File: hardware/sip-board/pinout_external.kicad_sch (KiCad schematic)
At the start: 24 parts, among them J2 Conn_01x10_Pin, J3 Conn_01x10_Pin, J4 Conn_01x10_Pin, J5 Conn_01x10_Pin

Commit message: WE REDOIN PCB
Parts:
- U10, U11, U12, U13, U4, U5, U6, U7, U8, U9: MPN (none) -> NXB0104GU12X
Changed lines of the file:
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@@
 			)
 		)
+		(property "MPN" "NXB0104GU12X"
+			(at 31.75 76.2 0)
+			(effects
+				(font
+					(size 1.27 1.27)
+				)
+				(hide yes)
+			)
+		)
 		(pin "5"
 		)
@@
 			)
 		)
+		(property "MPN" "NXB0104GU12X"
+			(at 118.11 144.78 0)
+			(effects
+				(font
+					(size 1.27 1.27)
+				)
+				(hide yes)
+			)
+		)
 		(pin "5"
 		)
@@
 			)
 		)
+		(property "MPN" "NXB0104GU12X"
+			(at 30.48 110.49 0)
+			(effects
+				(font
+					(size 1.27 1.27)
+				)
+				(hide yes)
+			)
+		)
 		(pin "5"
 		)
@@
 			)
 		)
+		(property "MPN" "NXB0104GU12X"
+			(at 119.38 110.49 0)
+			(effects
+				(font
+					(size 1.27 1.27)
+				)
+				(hide yes)
+			)
+		)
 		(pin "5"
 		)
@@
 			)
 		)
+		(property "MPN" "NXB0104GU12X"
+			(at 121.92 41.91 0)
+			(effects
+				(font
+					(size 1.27 1.27)
+				)
+				(hide yes)
+			)
+		)
 		(pin "5"
 		)
@@
 			)
 		)
+		(property "MPN" "NXB0104GU12X"
+			(at 120.65 76.2 0)
+			(effects
+				(font
+					(size 1.27 1.27)
+				)
+				(hide yes)
+			)
+		)
 		(pin "5"
 		)
@@
 			)
 		)
+		(property "MPN" "NXB0104GU12X"
+			(at 31.75 179.07 0)
+			(effects
+				(font
+					(size 1.27 1.27)
+				)
+				(hide yes)
+			)
+		)
 		(pin "5"
 		)
@@
 			)
 		)
+		(property "MPN" "NXB0104GU12X"
+			(at 33.02 41.91 0)
+			(effects
+				(font
+					(size 1.27 1.27)
+				)
+				(hide yes)
+			)
+		)
 		(pin "5"
 		)
@@
 			)
 		)
+		(property "MPN" "NXB0104GU12X"
+			(at 30.48 144.78 0)
+			(effects
+				(font
+					(size 1.27 1.27)
+				)
+				(hide yes)
+			)
+		)
 		(pin "5"
 		)
@@
 			(at 116.84 179.07 0)
 			(effects
+				(font
+					(size 1.27 1.27)
+				)
+				(hide yes)
+			)
+		)
+		(property "MPN" "NXB0104GU12X"
+			(at 116.84 179.07 0)
+			(effects

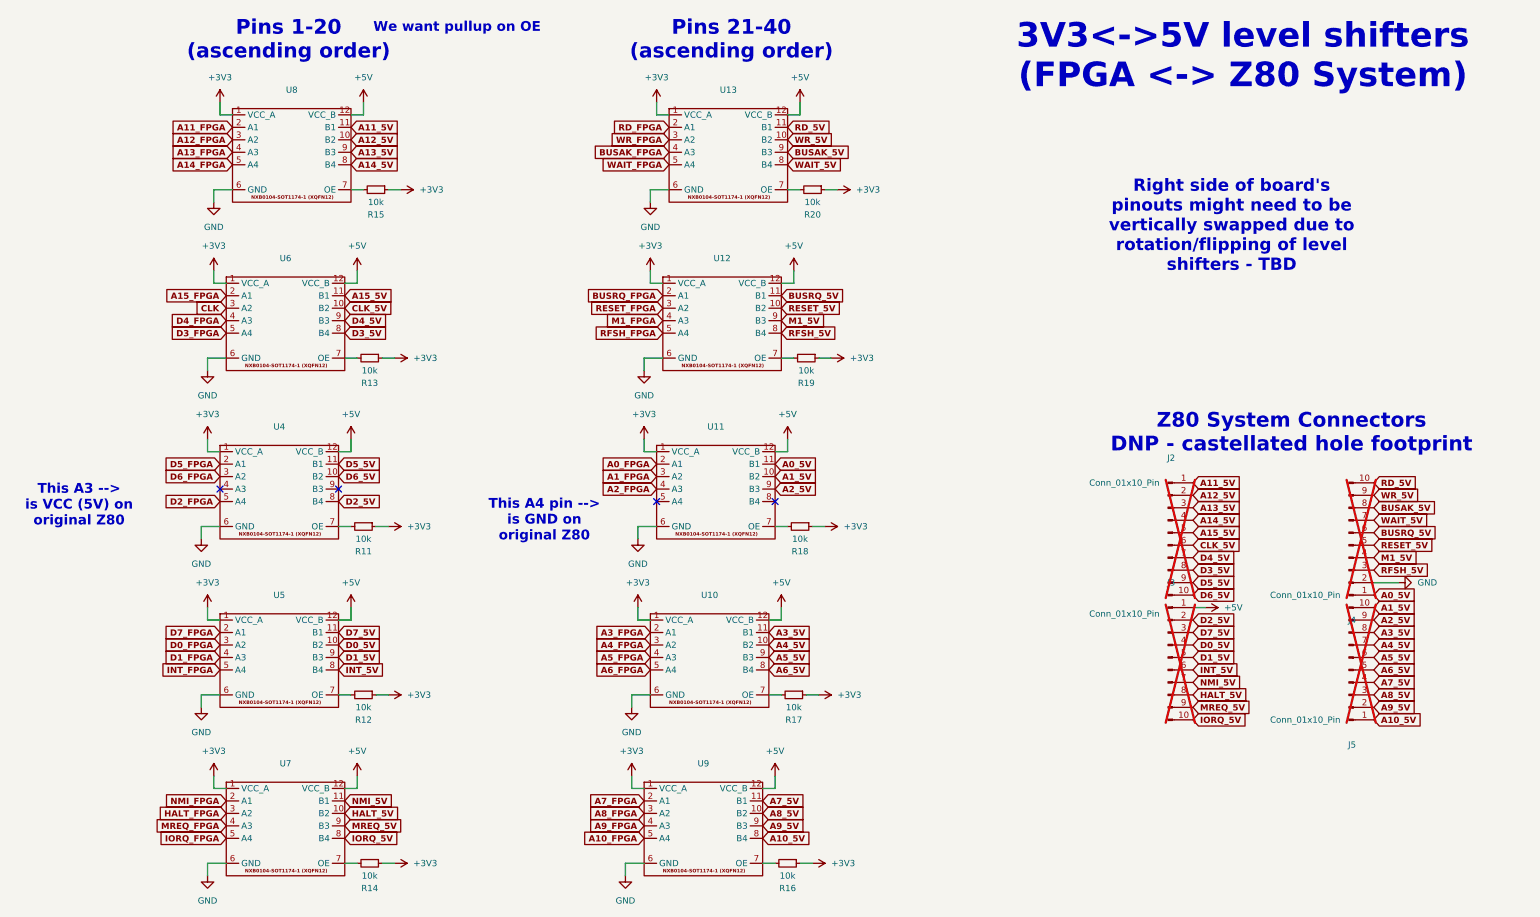
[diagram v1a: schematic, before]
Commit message: redo layout of sip (again), changed switching reg to be on surface, need to route, need to add 2 more layers for 5V plane
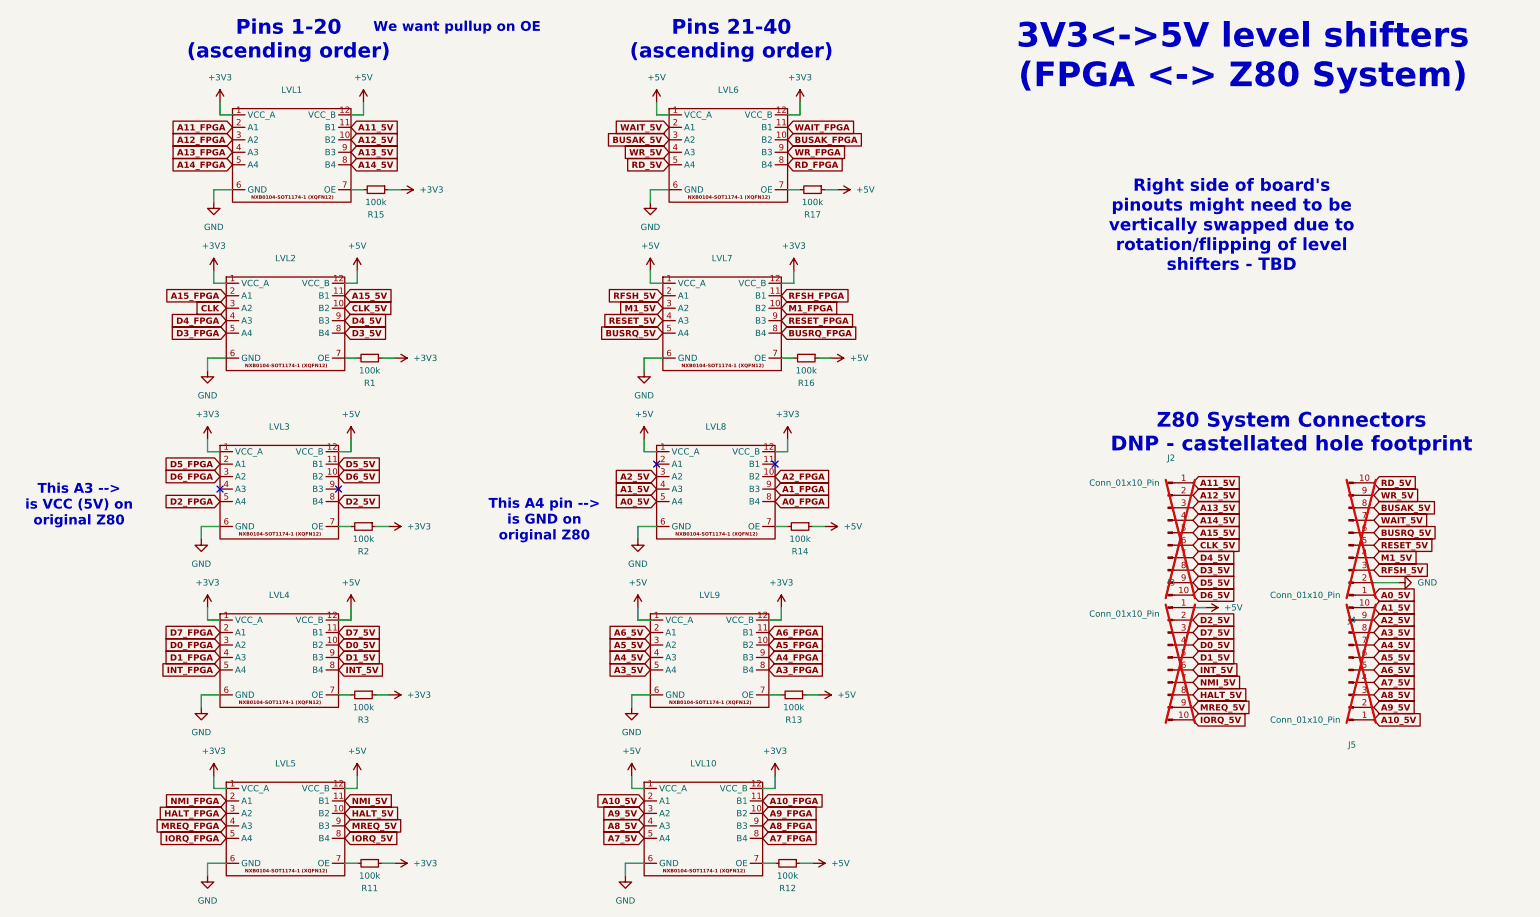
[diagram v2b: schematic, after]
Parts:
- removed R18, R19, R20: 10k, Resistor_SMD:R_0201_0603Metric, symbol Device:R_Small
- added R1, R2, R3: 100k, Resistor_SMD:R_0201_0603Metric, symbol Device:R_Small
- R11, R12, R13, R14, R15, R16, R17: value 10k -> 100k
- renumbered U8 to LVL1, U9 to LVL10, U6 to LVL2, U4 to LVL3, U5 to LVL4, U7 to LVL5, U13 to LVL6, U12 to LVL7, U11 to LVL8, U10 to LVL9
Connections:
- net +3V3: now also LVL10.12 (VCC_B), LVL6.12 (VCC_B), LVL7.12 (VCC_B), LVL8.12 (VCC_B), LVL9.12 (VCC_B), R1.1, R2.1, R3.1; no longer LVL10.1 (VCC_A), LVL6.1 (VCC_A), LVL7.1 (VCC_A), LVL8.1 (VCC_A), LVL9.1 (VCC_A), R12.1, R13.1, R14.1, R16.1, R17.1
- net +5V: now also LVL10.1 (VCC_A), LVL6.1 (VCC_A), LVL7.1 (VCC_A), LVL8.1 (VCC_A), LVL9.1 (VCC_A), R12.1, R13.1, R14.1, R16.1, R17.1; no longer LVL10.12 (VCC_B), LVL6.12 (VCC_B), LVL7.12 (VCC_B), LVL8.12 (VCC_B), LVL9.12 (VCC_B)
- net A0_5V: now also LVL8.5 (A4); no longer LVL8.11 (B1)
- net A0_FPGA: now also LVL8.8 (B4); no longer LVL8.2 (A1)
- net A10_5V: now also LVL10.2 (A1); no longer LVL10.8 (B4)
- net A10_FPGA: now also LVL10.11 (B1); no longer LVL10.5 (A4)
- net A1_5V: now also LVL8.4 (A3); no longer LVL8.10 (B2)
- net A1_FPGA: now also LVL8.9 (B3); no longer LVL8.3 (A2)
- net A2_5V: now also LVL8.3 (A2); no longer LVL8.9 (B3)
- net A2_FPGA: now also LVL8.10 (B2); no longer LVL8.4 (A3)
- net A3_5V: now also LVL9.5 (A4); no longer LVL9.11 (B1)
- net A3_FPGA: now also LVL9.8 (B4); no longer LVL9.2 (A1)
- net A4_5V: now also LVL9.4 (A3); no longer LVL9.10 (B2)
- net A4_FPGA: now also LVL9.9 (B3); no longer LVL9.3 (A2)
- net A5_5V: now also LVL9.3 (A2); no longer LVL9.9 (B3)
- net A5_FPGA: now also LVL9.10 (B2); no longer LVL9.4 (A3)
- net A6_5V: now also LVL9.2 (A1); no longer LVL9.8 (B4)
- net A6_FPGA: now also LVL9.11 (B1); no longer LVL9.5 (A4)
- net A7_5V: now also LVL10.5 (A4); no longer LVL10.11 (B1)
- net A7_FPGA: now also LVL10.8 (B4); no longer LVL10.2 (A1)
- net A8_5V: now also LVL10.4 (A3); no longer LVL10.10 (B2)
- net A8_FPGA: now also LVL10.9 (B3); no longer LVL10.3 (A2)
- net A9_5V: now also LVL10.3 (A2); no longer LVL10.9 (B3)
- net A9_FPGA: now also LVL10.10 (B2); no longer LVL10.4 (A3)
- net BUSAK_5V: now also LVL6.3 (A2); no longer LVL6.9 (B3)
- net BUSAK_FPGA: now also LVL6.10 (B2); no longer LVL6.4 (A3)
- net BUSRQ_5V: now also LVL7.5 (A4); no longer LVL7.11 (B1)
- net BUSRQ_FPGA: now also LVL7.8 (B4); no longer LVL7.2 (A1)
- net M1_5V: now also LVL7.3 (A2); no longer LVL7.9 (B3)
- net M1_FPGA: now also LVL7.10 (B2); no longer LVL7.4 (A3)
- net RD_5V: now also LVL6.5 (A4); no longer LVL6.11 (B1)
- net RD_FPGA: now also LVL6.8 (B4); no longer LVL6.2 (A1)
- net RESET_5V: now also LVL7.4 (A3); no longer LVL7.10 (B2)
- net RESET_FPGA: now also LVL7.9 (B3); no longer LVL7.3 (A2)
- net RFSH_5V: now also LVL7.2 (A1); no longer LVL7.8 (B4)
- net RFSH_FPGA: now also LVL7.11 (B1); no longer LVL7.5 (A4)
- net WAIT_5V: now also LVL6.2 (A1); no longer LVL6.8 (B4)
- net WAIT_FPGA: now also LVL6.11 (B1); no longer LVL6.5 (A4)
- net WR_5V: now also LVL6.4 (A3); no longer LVL6.10 (B2)
- net WR_FPGA: now also LVL6.9 (B3); no longer LVL6.3 (A2)
- net at LVL2.7 (OE): now also R1.2; no longer R13.2
- net at LVL9.7 (OE): now also R13.2; no longer R17.2
- net at LVL5.7 (OE): now also R11.2; no longer R14.2
- net at LVL3.7 (OE): now also R2.2; no longer R11.2
- net at R16.2: now also LVL7.7 (OE); no longer LVL10.7 (OE)
- net at LVL8.7 (OE): now also R14.2
- net at LVL6.7 (OE): now also R17.2
- net at LVL4.7 (OE): now also R3.2; no longer R12.2
- new net: LVL10.7 (OE), R12.2

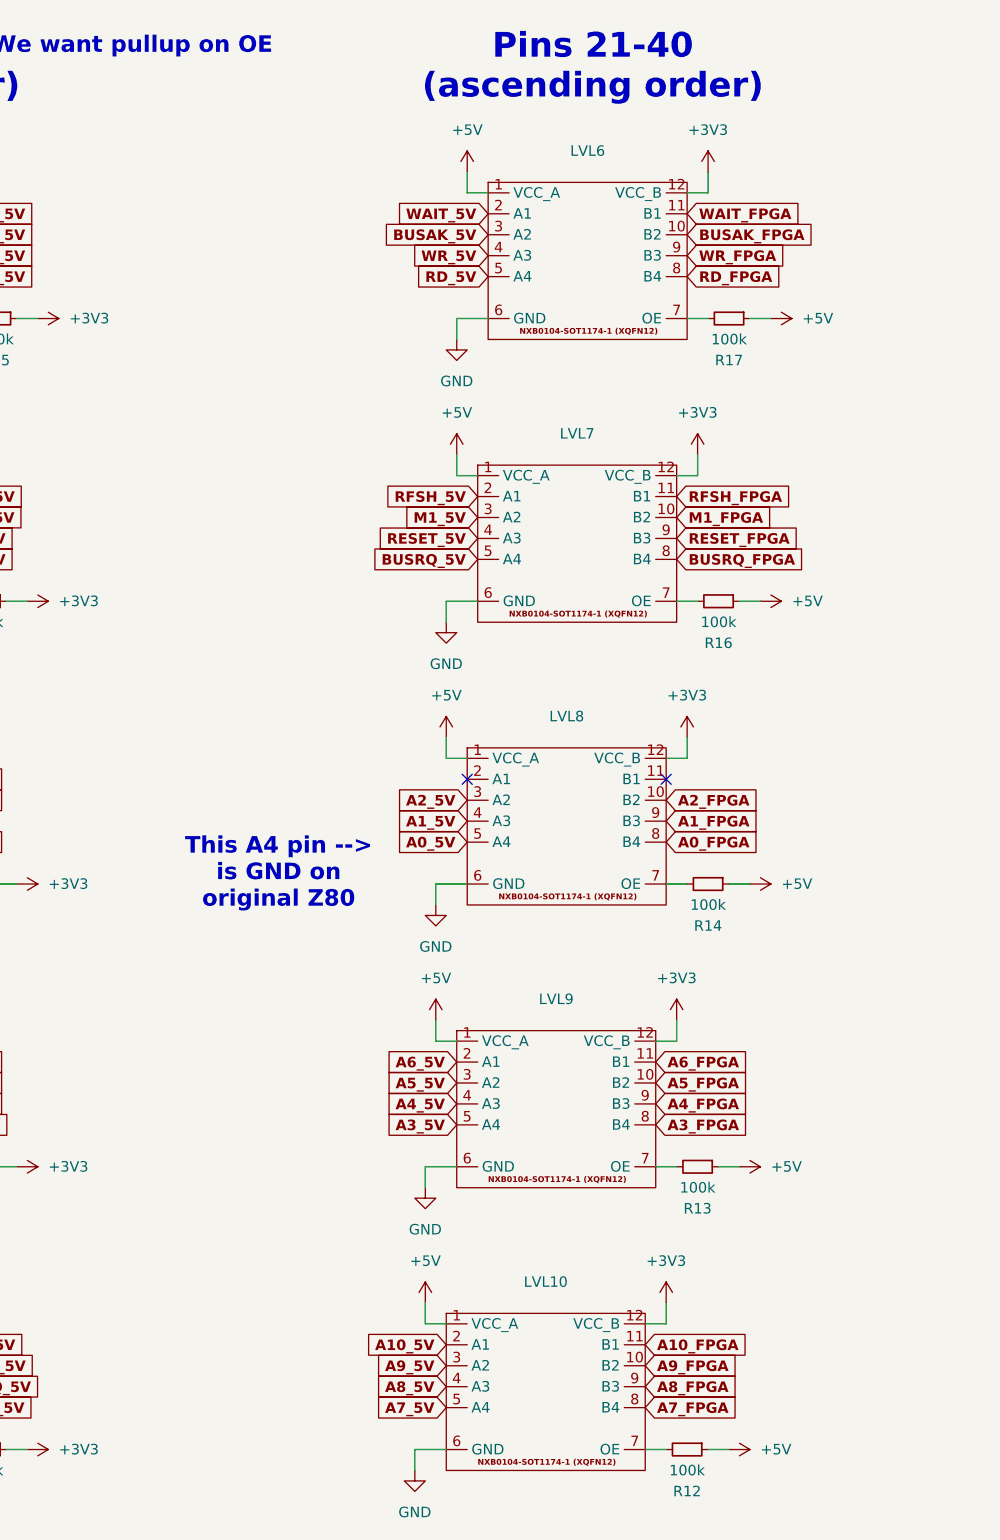
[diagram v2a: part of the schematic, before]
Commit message: sip vreg redo, connect level shifters to outside pins
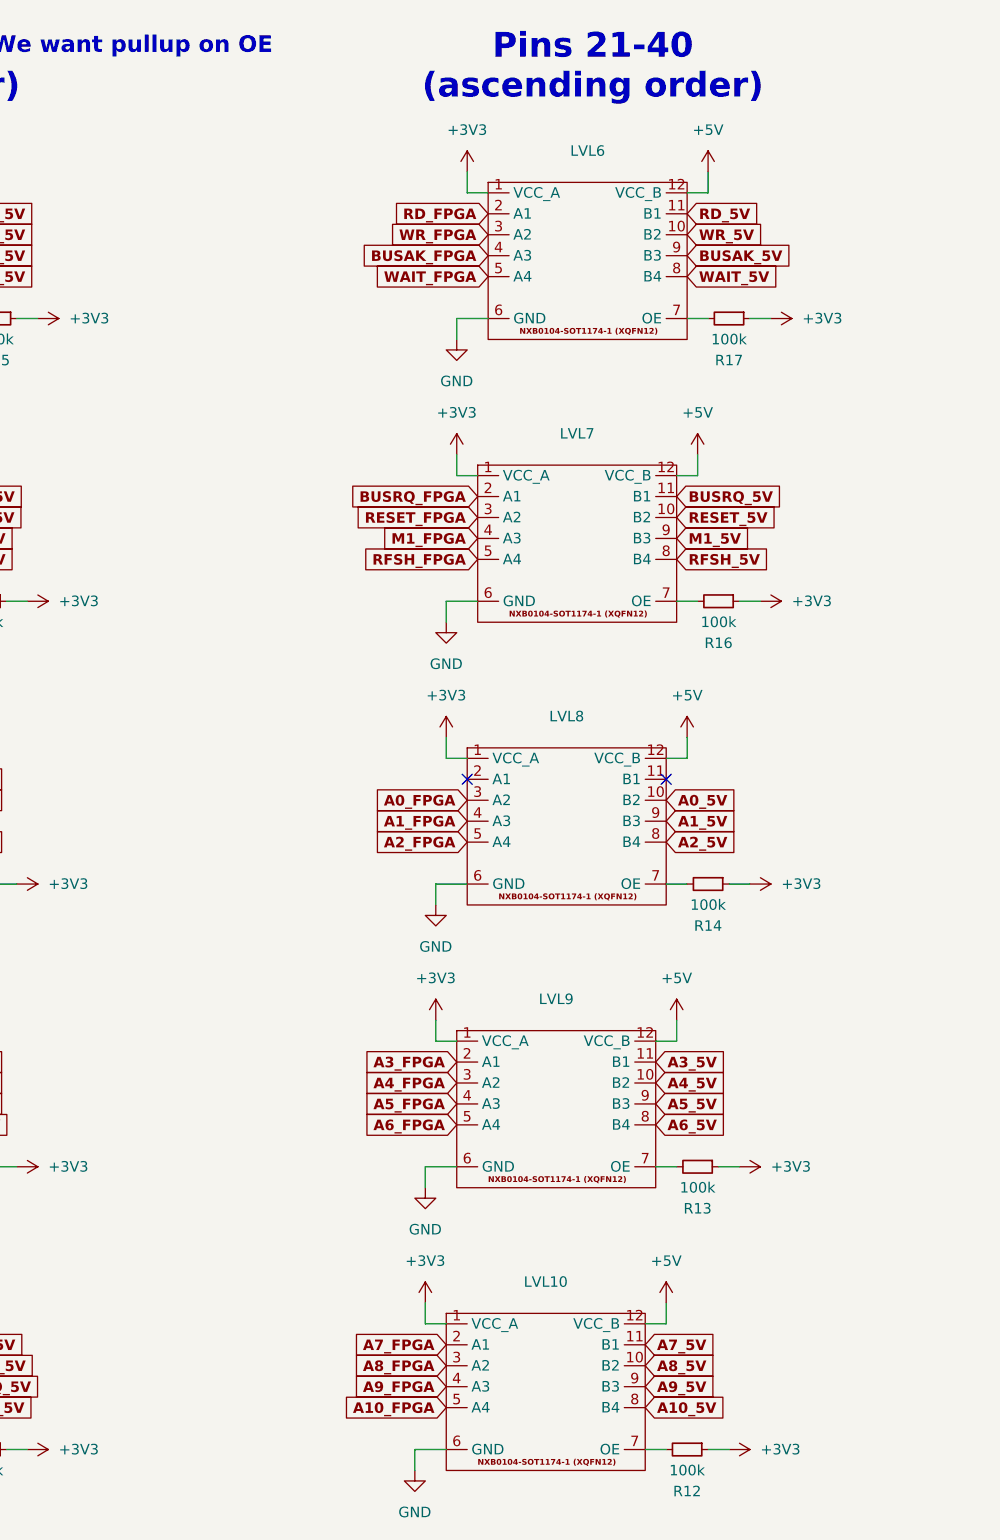
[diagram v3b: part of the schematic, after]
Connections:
- net +3V3: now also LVL10.1 (VCC_A), LVL6.1 (VCC_A), LVL7.1 (VCC_A), LVL8.1 (VCC_A), LVL9.1 (VCC_A), R12.1, R13.1, R14.1, R16.1, R17.1; no longer LVL10.12 (VCC_B), LVL6.12 (VCC_B), LVL7.12 (VCC_B), LVL8.12 (VCC_B), LVL9.12 (VCC_B)
- net +5V: now also LVL10.12 (VCC_B), LVL6.12 (VCC_B), LVL7.12 (VCC_B), LVL8.12 (VCC_B), LVL9.12 (VCC_B); no longer LVL10.1 (VCC_A), LVL6.1 (VCC_A), LVL7.1 (VCC_A), LVL8.1 (VCC_A), LVL9.1 (VCC_A), R12.1, R13.1, R14.1, R16.1, R17.1
- net A0_5V: now also LVL8.10 (B2); no longer LVL8.5 (A4)
- net A0_FPGA: now also LVL8.3 (A2); no longer LVL8.8 (B4)
- net A10_5V: now also LVL10.8 (B4); no longer LVL10.2 (A1)
- net A10_FPGA: now also LVL10.5 (A4); no longer LVL10.11 (B1)
- net A1_5V: now also LVL8.9 (B3); no longer LVL8.4 (A3)
- net A1_FPGA: now also LVL8.4 (A3); no longer LVL8.9 (B3)
- net A2_5V: now also LVL8.8 (B4); no longer LVL8.3 (A2)
- net A2_FPGA: now also LVL8.5 (A4); no longer LVL8.10 (B2)
- net A3_5V: now also LVL9.11 (B1); no longer LVL9.5 (A4)
- net A3_FPGA: now also LVL9.2 (A1); no longer LVL9.8 (B4)
- net A4_5V: now also LVL9.10 (B2); no longer LVL9.4 (A3)
- net A4_FPGA: now also LVL9.3 (A2); no longer LVL9.9 (B3)
- net A5_5V: now also LVL9.9 (B3); no longer LVL9.3 (A2)
- net A5_FPGA: now also LVL9.4 (A3); no longer LVL9.10 (B2)
- net A6_5V: now also LVL9.8 (B4); no longer LVL9.2 (A1)
- net A6_FPGA: now also LVL9.5 (A4); no longer LVL9.11 (B1)
- net A7_5V: now also LVL10.11 (B1); no longer LVL10.5 (A4)
- net A7_FPGA: now also LVL10.2 (A1); no longer LVL10.8 (B4)
- net A8_5V: now also LVL10.10 (B2); no longer LVL10.4 (A3)
- net A8_FPGA: now also LVL10.3 (A2); no longer LVL10.9 (B3)
- net A9_5V: now also LVL10.9 (B3); no longer LVL10.3 (A2)
- net A9_FPGA: now also LVL10.4 (A3); no longer LVL10.10 (B2)
- net BUSAK_5V: now also LVL6.9 (B3); no longer LVL6.3 (A2)
- net BUSAK_FPGA: now also LVL6.4 (A3); no longer LVL6.10 (B2)
- net BUSRQ_5V: now also LVL7.11 (B1); no longer LVL7.5 (A4)
- net BUSRQ_FPGA: now also LVL7.2 (A1); no longer LVL7.8 (B4)
- net M1_5V: now also LVL7.9 (B3); no longer LVL7.3 (A2)
- net M1_FPGA: now also LVL7.4 (A3); no longer LVL7.10 (B2)
- net RD_5V: now also LVL6.11 (B1); no longer LVL6.5 (A4)
- net RD_FPGA: now also LVL6.2 (A1); no longer LVL6.8 (B4)
- net RESET_5V: now also LVL7.10 (B2); no longer LVL7.4 (A3)
- net RESET_FPGA: now also LVL7.3 (A2); no longer LVL7.9 (B3)
- net RFSH_5V: now also LVL7.8 (B4); no longer LVL7.2 (A1)
- net RFSH_FPGA: now also LVL7.5 (A4); no longer LVL7.11 (B1)
- net WAIT_5V: now also LVL6.8 (B4); no longer LVL6.2 (A1)
- net WAIT_FPGA: now also LVL6.5 (A4); no longer LVL6.11 (B1)
- net WR_5V: now also LVL6.10 (B2); no longer LVL6.4 (A3)
- net WR_FPGA: now also LVL6.3 (A2); no longer LVL6.9 (B3)
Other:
- note removed: "This A4 pin --> is GND on original Z80"
